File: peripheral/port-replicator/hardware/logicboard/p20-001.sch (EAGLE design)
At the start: 64 parts, among them IC1 74LS07N, IC11 74LS153D, IC12 LTC485S, IC13 LTC485S, IC2 4066N, J1 MKR, J11 Qwiic, J12 Qwiic, J13 Qwiic, J14 Qwiic, J2 GPIO, J3 Vout, J4 RLY, J5 SPI, J6 LED, K1 G5V1, T1 2SC1815, U1 DS18B20

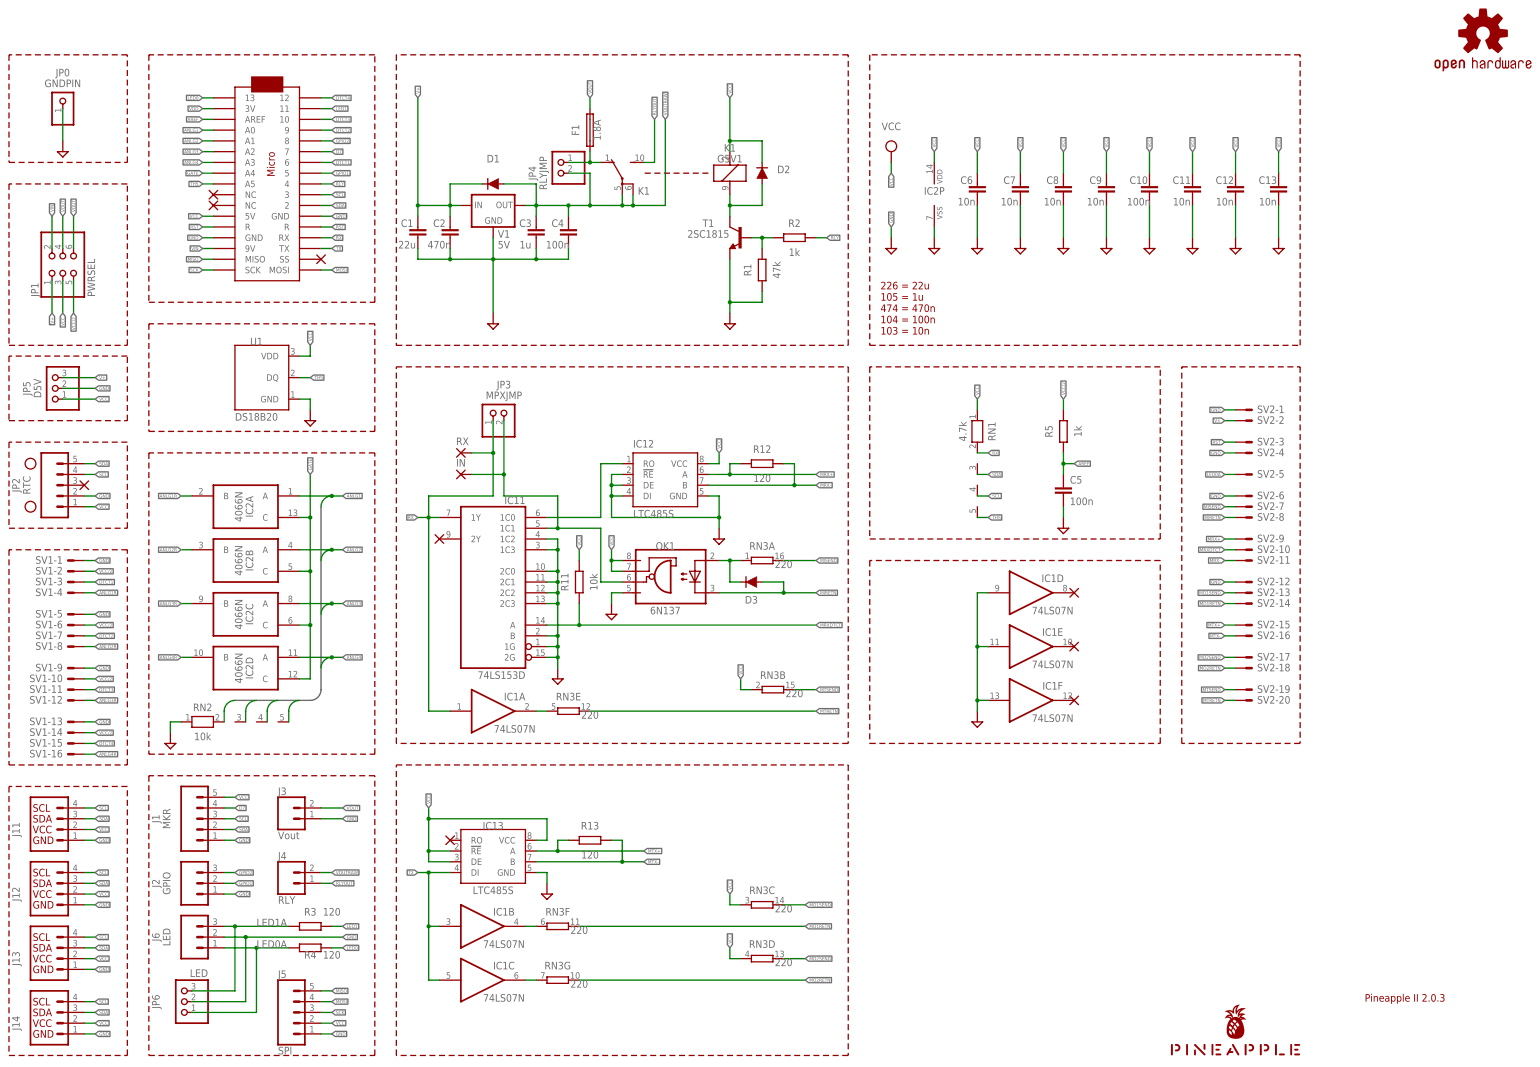
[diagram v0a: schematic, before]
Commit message: Cleared unnecessary parts.
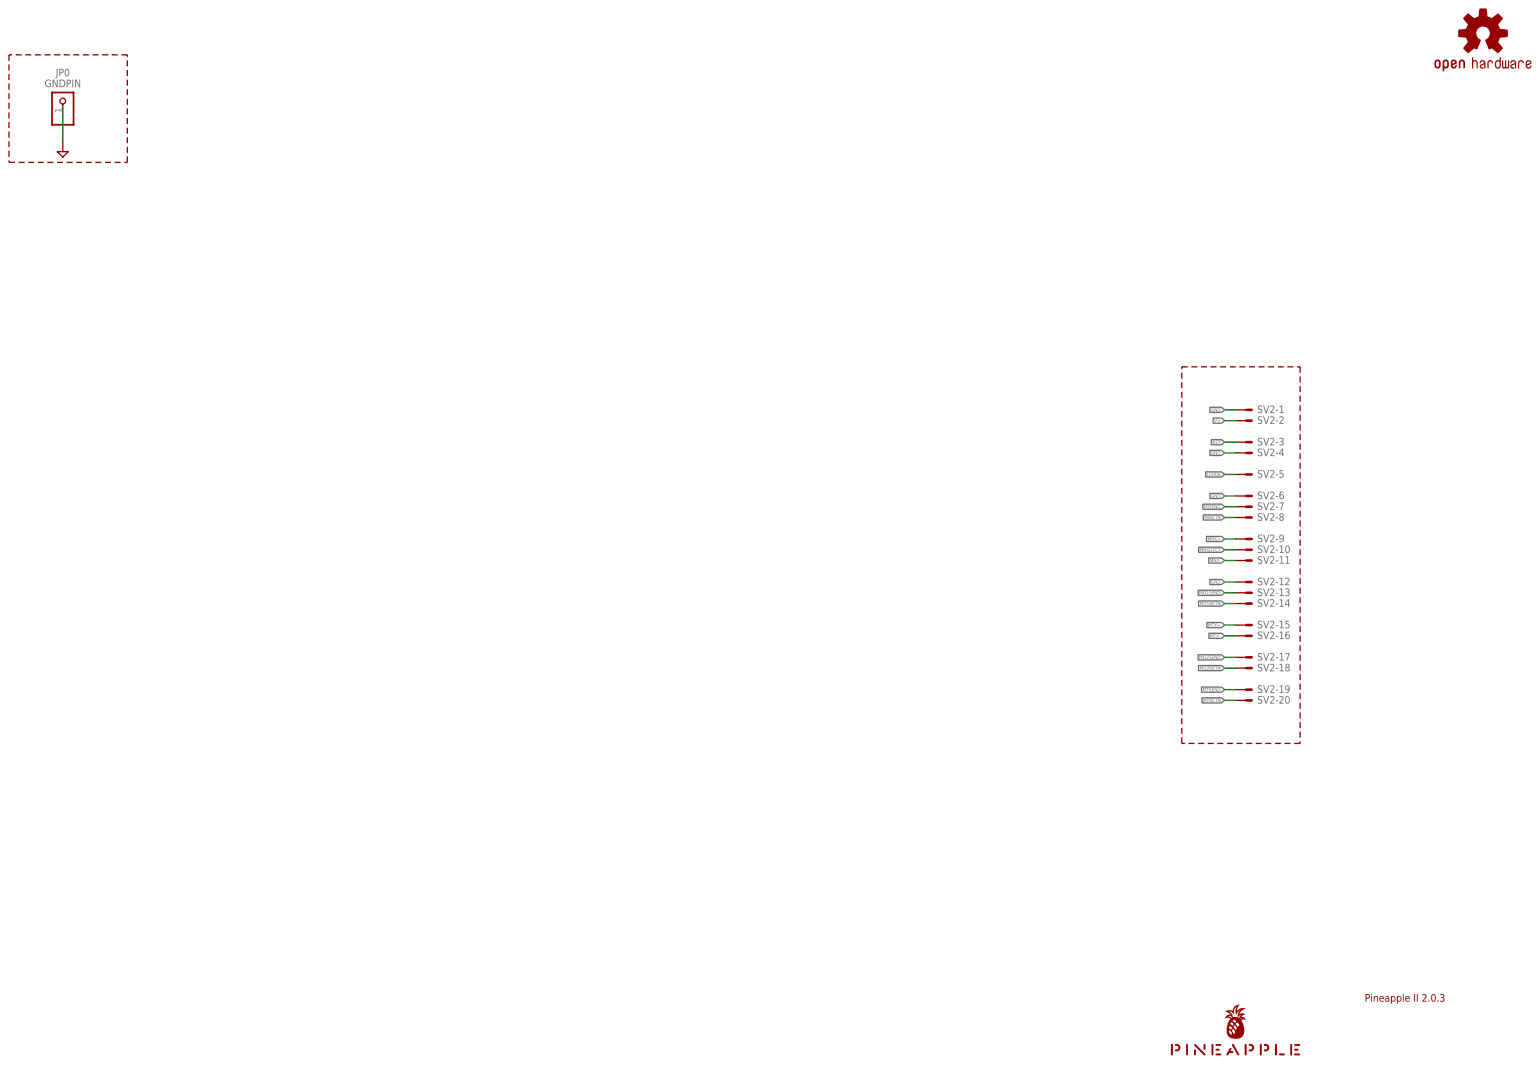
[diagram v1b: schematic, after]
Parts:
- removed C1: 22u, rcl:C-EU025-050X050
- removed C10, C4, C5: 100n, rcl:C-EU025-024X044
- removed C11, C12, C13: 10n, rcl:C-EUC2012
- removed C2: 470n, rcl:C-EU050-024X044
- removed C3: 1u, rcl:C-EU050-024X044
- removed C6, C7, C8, C9: 10n, resistor:C-EU025-024X044
- removed D1, D2, D3: DIODE-1N4148, SparkFun-DiscreteSemi:DIODE-1N4148
- removed F1: 1.8A, fuse:TE5
- removed H1, H2: STAND-OFF, SparkFun-Hardware:STAND-OFF
- removed IC1: 74LS07N, 74xx-us:74LS07N
- removed IC11: 74LS153D, 74xx-us:74LS153D
- removed IC12, IC13: LTC485S, linear-technology:LTC485S
- removed IC2: 4066N, 40xx:4066N
- removed IN, RX: (no value), wirepad:SMD2
- removed J1: MKR, SparkFun-Connectors:CONN_05JST
- removed J11, J12, J13, J14: Qwiic, SparkFun-Connectors:QWIIC_CONNECTORJS-1MM
- removed J2: GPIO, SparkFun-Connectors:CONN_03JST-PTH
- removed J3: Vout, SparkFun-Connectors:CONN_02JST-PTH-2
- removed J4: RLY, SparkFun-Connectors:CONN_02JST-PTH-2
- removed J5: SPI, SparkFun-Connectors:CONN_05JST-VERT
- removed J6: LED, SparkFun-Connectors:CONN_03JST-PTH
- removed JP1: PWRSEL, pinhead:PINHD-2X3
- removed JP2: RTC, SparkFun-Connectors:CONN_05
- removed JP3: MPXJMP, pinhead:PINHD-1X2
- removed JP4: RLYJMP, pinhead:PINHD-1X2
- removed JP5: D5V, pinhead:PINHD-1X3
- removed JP6: LED, pinhead:PINHD-1X3
- removed K1: G5V1, relay:G5V1
- removed MC1: ARDUINOMICRO, adafruit:ARDUINOMICRO
- removed OK1: 6N137, optocoupler:6N137
- removed R1: 47k, resistor:R-EU_0204/5
- removed R11: 10k, rcl:R-EU_M2012
- removed R12, R13: 120, rcl:R-EU_M2012
- removed R2, R5: 1k, resistor:R-EU_0204/5
- removed R3, R4: 120, resistor:R-EU_0204/5
- removed RN1: 4.7k, resistor-net:RN04
- removed RN2: 10k, resistor-net:RN04
- removed RN3: 220, resistor-dil:8R-N
- removed SV1: (no value), con-ml:ML16LE
- removed T1: 2SC1815, transistor:2SC1815
- removed U1: DS18B20, SparkFun-Sensors:DS18B20
- removed V1: 5V, v-reg:78XXL
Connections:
- removed net ANLG1: IC2A.A, MC1.A0, RN2.2
- removed net ANLG1R: IC2A.B, SV1-4.S
- removed net ANLG2: IC2B.A, MC1.A1, RN2.3
- removed net ANLG2R: IC2B.B, SV1-8.S
- removed net ANLG3: IC2C.A, MC1.A2, RN2.4
- removed net ANLG3R: IC2C.B, SV1-12.S
- removed net ANLG4: IC2D.A, MC1.A3, RN2.5
- removed net ANLG4R: IC2D.B, SV1-16.S
- removed net AREF: C5.1, MC1.AREF, R5.1
- removed net D7: J1.4, MC1.7
- removed net DTCT1: MC1.6, SV1-3.S
- removed net DTCT2: MC1.9, SV1-7.S
- removed net DTCT3: MC1.10, SV1-11.S
- removed net DTCT4: MC1.12, SV1-15.S
- removed net GATE: IC2A.C, IC2B.C, IC2C.C, IC2D.C, MC1.A4
- removed net GPIO1: J2.2, MC1.5
- removed net GPIO2: J2.3, MC1.8
- removed net LED0: MC1.13, R4.2
- removed net LED1: MC1.11, R3.2
- removed net LED1A: J6.3, JP6.3, R3.1
- removed net MIDIINSND: D3.C, OK1.A, RN3A.1
- removed net MIN: IC11A.1C1, IN.P, JP3.2, OK1.VO
- removed net MISO: J5.5, MC1.MISO
- removed net MO1: IC1B.O, RN3F.1
- removed net MO2: IC1C.O, RN3G.1
- removed net MOSI: J5.4, MC1.MOSI
- removed net MRX: IC11A.1C0, IC12.RO
- removed net MT: IC1A.O, RN3E.1
- removed net RLY: MC1.4, R2.2
- removed net RLYDRV: R1.2, R2.1, T1.B
- removed net RLYOUT: J4.1, K12.S
- removed net RLYSNK: D2.A, K11.2, T1.C
- removed net RX: IC11A.1Y, IC1A.I, JP3.1, MC1.RX, RN1.2, RX.P
- removed net SCK: J5.3, MC1.SCK
- removed net SCL: J1.3, J11.SCL, J12.SCL, J13.SCL, J14.SCL, JP2.4, MC1.3, RN1.4
- removed net SDA: J1.2, J11.SDA, J12.SDA, J13.SDA, J14.SDA, JP2.5, MC1.2, RN1.3
- removed net THS: MC1.A5, RN1.5, U1.DQ
- removed net TX: IC13.DI, IC1B.I, IC1C.I, MC1.TX
- removed net VCC: C10.1, C11.1, C12.1, C13.1, C6.1, C7.1, C8.1, C9.1, D2.C, IC12.VCC, IC13.!RE, IC13.DE, IC13.VCC, IC2P.VDD, J1.5, J11.VCC, J12.VCC, J13.VCC, J14.VCC, J5.2, JP1.3, JP2.1, JP5.1, K11.1, MC1.5V, OK1.VCC, OK1.VE, R11.2, RN1.1, RN3B.1, RN3C.1, RN3D.1, U1.VDD
- removed net VCC/2: JP1.5, R5.2, SV1-10.S, SV1-14.S, SV1-2.S, SV1-6.S
- removed net VDD: MC1.3V
- removed net VIN: JP1.2, MC1.9V
- removed net VOUT: F1.2, J3.2, JP1.4, JP1.6
- removed net VOUTRAW: C3.1, C4.1, D1.A, J4.2, JP4.2, K12.P, K12.P@1, V1.OUT
- removed net VOUTRAW2: F1.1, JP4.1, K12.O
- net GND: no longer C1.2, C10.2, C11.2, C12.2, C13.2, C2.2, C3.2, C4.2, C5.2, C6.2, C7.2, C8.2, C9.2, IC11A.1C2, IC11A.1C3, IC11A.1G, IC11A.2C0, IC11A.2C1, IC11A.2C2, IC11A.2C3, IC11A.2G, IC11A.B, IC12.!RE, IC12.DE, IC12.DI, IC12.GND, IC13.GND, IC1D.I, IC1E.I, IC1F.I, IC2P.VSS, J1.1, J11.GND, J12.GND, J13.GND, J14.GND, J2.1, J3.1, J5.1, J6.2, JP2.2, JP5.2, JP6.2, MC1.GND, MC1.GND@1, OK1.GND, R1.1, RN2.1, SV1-1.S, SV1-13.S, SV1-5.S, SV1-9.S, T1.E, U1.GND, V1.GND
- net LED0A: no longer J6.1, JP6.1, R4.1
- net MIRETN: no longer D3.A, OK1.C
- net MISEND: no longer RN3A.2
- net MO1RETN: no longer RN3F.2
- net MO1SEND: no longer RN3C.2
- net MO2RETN: no longer RN3G.2
- net MO2SEND: no longer RN3D.2
- net MRX+: no longer IC12.A, R12.1
- net MRX-: no longer IC12.B, R12.2
- net MRXDTCT: no longer IC11A.A, R11.1
- net MTRETN: no longer RN3E.2
- net MTSEND: no longer RN3B.2
- net MTX+: no longer IC13.A, R13.1
- net MTX-: no longer IC13.B, R13.2
- net RST: no longer MC1.R@1, MC1.R@2
- net V+: no longer C1.1, C2.1, D1.C, JP1.1, JP5.3, V1.IN
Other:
- note removed: "226 = 22u 105 = 1u 474 = 470n 104 = 100n 103 = 10n"

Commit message: Parts only. No connection.
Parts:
- added J0: (no value), con-jack:JACK-PLUG0
- added J1, J2, J3: DIN5, SparkFun-Connectors:DIN5
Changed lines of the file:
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@@
 <part name="JP0" library="pinhead" library_urn="urn:adsk.eagle:library:325" deviceset="PINHD-1X1" device="" package3d_urn="urn:adsk.eagle:package:22485/2" value="GNDPIN"/>
 <part name="SUPPLY33" library="supply2" deviceset="GND" device=""/>
+<part name="J1" library="SparkFun-Connectors" library_urn="urn:adsk.eagle:library:513" deviceset="DIN5" device="" package3d_urn="urn:adsk.eagle:package:38294/1"/>
+<part name="J2" library="SparkFun-Connectors" library_urn="urn:adsk.eagle:library:513" deviceset="DIN5" device="" package3d_urn="urn:adsk.eagle:package:38294/1"/>
+<part name="J3" library="SparkFun-Connectors" library_urn="urn:adsk.eagle:library:513" deviceset="DIN5" device="" package3d_urn="urn:adsk.eagle:package:38294/1"/>
+<part name="J0" library="con-jack" library_urn="urn:adsk.eagle:library:154" deviceset="JACK-PLUG" device="0" package3d_urn="urn:adsk.eagle:package:7492/1"/>
 </parts>
 <sheets>
@@
 </instance>
 <instance part="SUPPLY33" gate="GND" x="35.56" y="220.98" smashed="yes"/>
+<instance part="J1" gate="G$1" x="35.56" y="190.5" smashed="yes">
+<attribute name="NAME" x="35.56" y="184.912" size="1.778" layer="95" font="vector" align="bottom-center"/>
+<attribute name="VALUE" x="35.56" y="182.626" size="1.778" layer="96" font="vector" align="top-center"/>
+</instance>
+<instance part="J2" gate="G$1" x="35.56" y="165.1" smashed="yes">
+<attribute name="NAME" x="35.56" y="159.512" size="1.778" layer="95" font="vector" align="bottom-center"/>
+<attribute name="VALUE" x="35.56" y="157.226" size="1.778" layer="96" font="vector" align="top-center"/>
+</instance>
+<instance part="J3" gate="G$1" x="35.56" y="142.24" smashed="yes">
+<attribute name="NAME" x="35.56" y="136.652" size="1.778" layer="95" font="vector" align="bottom-center"/>
+<attribute name="VALUE" x="35.56" y="134.366" size="1.778" layer="96" font="vector" align="top-center"/>
+</instance>
+<instance part="J0" gate="G$1" x="38.1" y="116.84" smashed="yes">
+<attribute name="NAME" x="30.48" y="121.92" size="1.778" layer="95"/>
+<attribute name="VALUE" x="30.48" y="111.76" size="1.778" layer="96"/>
+</instance>
 </instances>
 <busses>
